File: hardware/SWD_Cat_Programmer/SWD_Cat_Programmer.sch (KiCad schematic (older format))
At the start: 19 parts

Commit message: Bom and footprints added
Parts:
- C1, C2, C3, C4, C5: renamed from C?; footprint (none) -> Capacitor_SMD:C_0603_1608Metric_Pad1.05x0.95mm_HandSolder
- D1: renamed from D?; footprint (none) -> LED_SMD:LED_0805_2012Metric
- J1: renamed from J?; footprint (none) -> Connector_PinHeader_2.54mm:PinHeader_2x05_P2.54mm_Vertical
- P1: renamed from P?; footprint (none) -> Connectors:C393939
- R1, R2, R3, R4, R5, R6, R7: renamed from R?; footprint (none) -> Resistor_SMD:R_0603_1608Metric_Pad1.05x0.95mm_HandSolder
- SW1, SW2: renamed from SW?; footprint (none) -> Button_Switch_SMD:SW_SPST_TL3342
- U1: renamed from U?; footprint (none) -> Package_SO:SOP-16_4.55x10.3mm_P1.27mm; symbol Electronic_Cats:CH552G -> SWD_Cat_Programmer-rescue:CH552G-Electronic_Cats
- gave numbers to parts that had none: 1

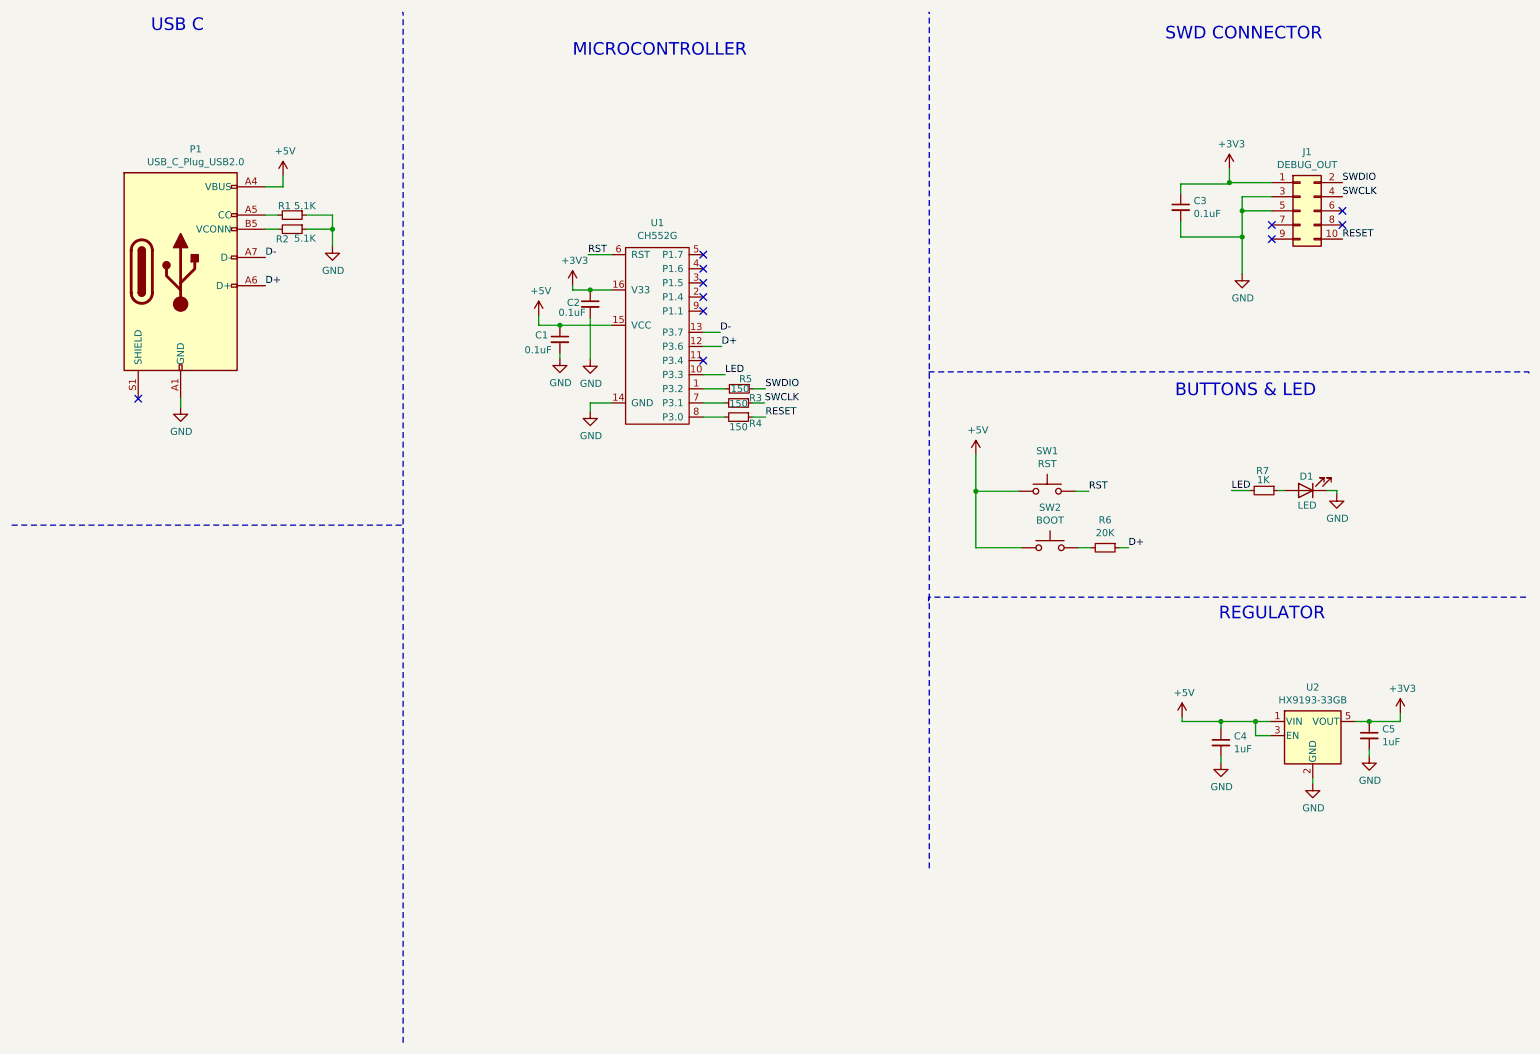
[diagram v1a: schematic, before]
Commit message: capacitors modified
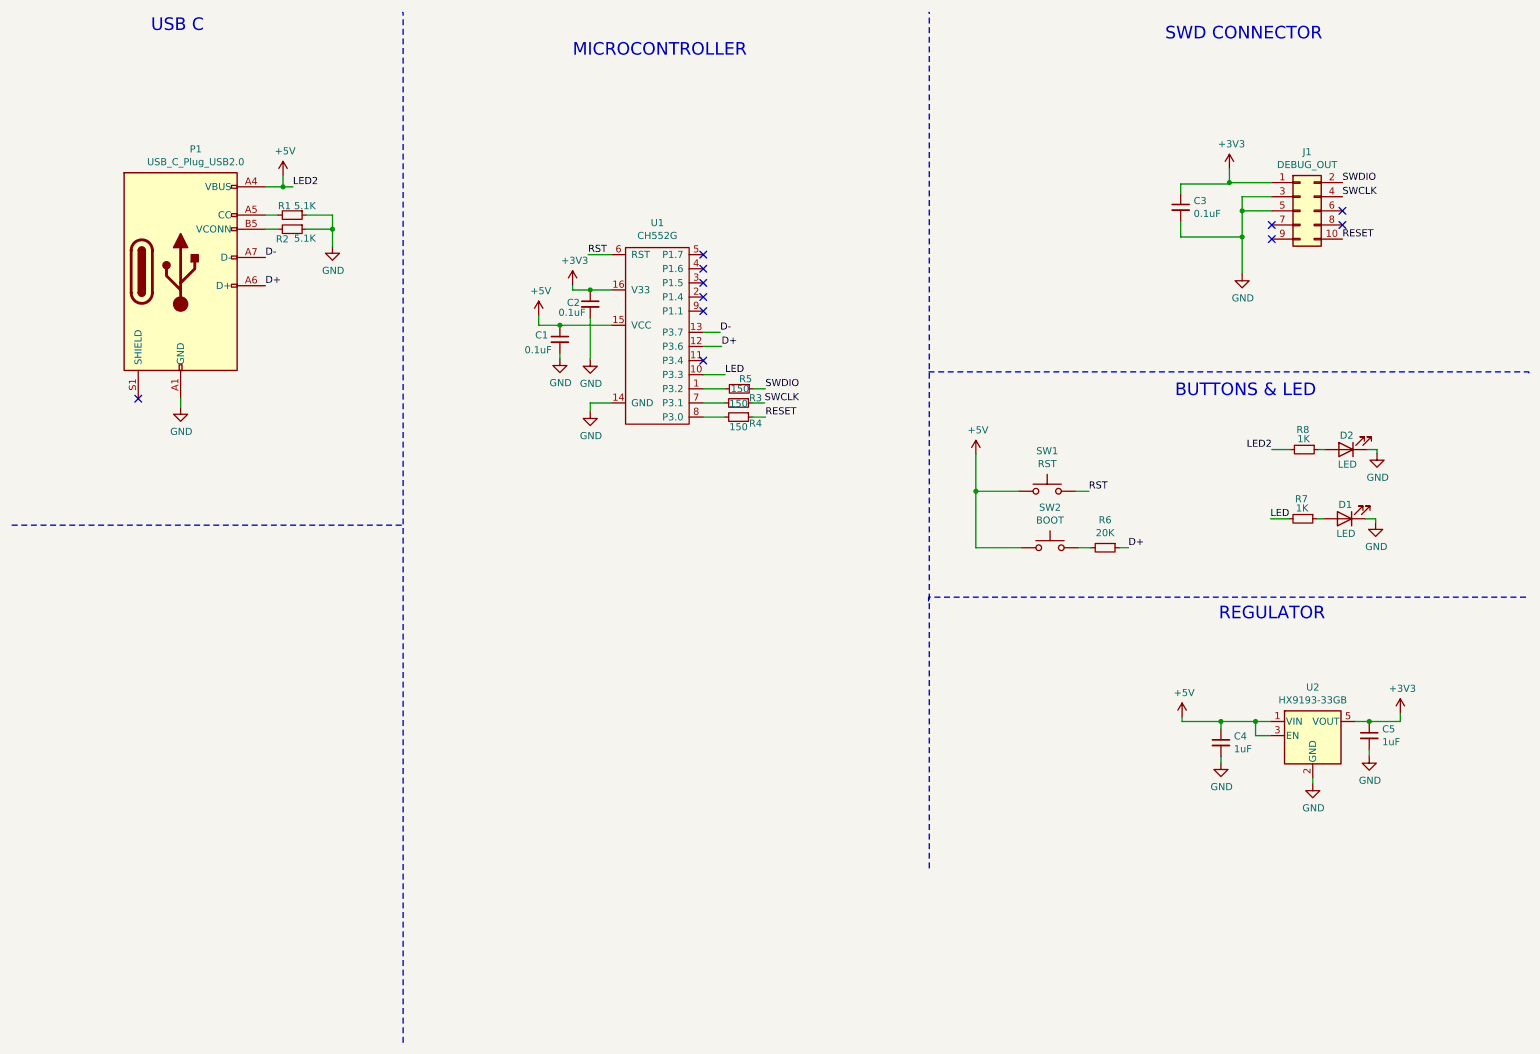
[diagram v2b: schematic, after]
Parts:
- added D2: LED, LED_SMD:LED_0805_2012Metric, symbol Device:LED
- added R8: 1K, Resistor_SMD:R_0805_2012Metric_Pad1.15x1.40mm_HandSolder, symbol Device:R_Small
- C1, C2, C3, C4, C5: footprint Capacitor_SMD:C_0603_1608Metric_Pad1.05x0.95mm_HandSolder -> Capacitor_SMD:C_0805_2012Metric_Pad1.15x1.40mm_HandSolder
- R1, R2, R3, R4, R5, R6, R7: footprint Resistor_SMD:R_0603_1608Metric_Pad1.05x0.95mm_HandSolder -> Resistor_SMD:R_0805_2012Metric_Pad1.15x1.40mm_HandSolder
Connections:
- net +5V: now also R8.2
- net GND: now also D2.1 (K)
- new net: D2.2 (A), R8.1
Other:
- moved on the sheet: D1, R7
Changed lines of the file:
@@
 F 0 "C3" H 8852 1901 50  0000 L CNN
 F 1 "0.1uF" H 8852 1810 50  0000 L CNN
-F 2 "Capacitor_SMD:C_0603_1608Metric_Pad1.05x0.95mm_HandSolder" H 8760 1855 50  0001 C CNN
+F 2 "Capacitor_SMD:C_0805_2012Metric_Pad1.15x1.40mm_HandSolder" H 8760 1855 50  0001 C CNN
 F 3 "~" H 8760 1855 50  0001 C CNN
 	1    8760 1855
@@
 F 0 "R1" V 2405 1855 50  0000 C CNN
 F 1 "5.1K" V 2405 2000 50  0000 C CNN
-F 2 "Resistor_SMD:R_0603_1608Metric_Pad1.05x0.95mm_HandSolder" H 2470 1910 50  0001 C CNN
+F 2 "Resistor_SMD:R_0805_2012Metric_Pad1.15x1.40mm_HandSolder" H 2470 1910 50  0001 C CNN
 F 3 "~" H 2470 1910 50  0001 C CNN
 	1    2470 1910
@@
 F 0 "C1" H 4190 2820 50  0000 L CNN
 F 1 "0.1uF" H 4115 2715 50  0000 L CNN
-F 2 "Capacitor_SMD:C_0603_1608Metric_Pad1.05x0.95mm_HandSolder" H 4365 2790 50  0001 C CNN
+F 2 "Capacitor_SMD:C_0805_2012Metric_Pad1.15x1.40mm_HandSolder" H 4365 2790 50  0001 C CNN
 F 3 "~" H 4365 2790 50  0001 C CNN
 	1    4365 2790
@@
 F 0 "C2" H 4415 2550 50  0000 L CNN
 F 1 "0.1uF" H 4355 2480 50  0000 L CNN
-F 2 "Capacitor_SMD:C_0603_1608Metric_Pad1.05x0.95mm_HandSolder" H 4580 2540 50  0001 C CNN
+F 2 "Capacitor_SMD:C_0805_2012Metric_Pad1.15x1.40mm_HandSolder" H 4580 2540 50  0001 C CNN
 F 3 "~" H 4580 2540 50  0001 C CNN
 	1    4580 2540
@@
 F 0 "R2" V 2540 1940 50  0000 C CNN
 F 1 "5.1K" V 2535 2100 50  0000 C CNN
-F 2 "Resistor_SMD:R_0603_1608Metric_Pad1.05x0.95mm_HandSolder" H 2470 2010 50  0001 C CNN
+F 2 "Resistor_SMD:R_0805_2012Metric_Pad1.15x1.40mm_HandSolder" H 2470 2010 50  0001 C CNN
 F 3 "~" H 2470 2010 50  0001 C CNN
 	1    2470 2010
@@
 $EndComp
 Wire Wire Line
-	9120 3860 9250 3860
+	9395 4060 9525 4060
 $Comp
 L Device:R_Small R7
 U 1 1 5F275B65
-P 9350 3860
-F 0 "R7" V 9210 3850 50  0000 C CNN
-F 1 "1K" V 9275 3855 50  0000 C CNN
-F 2 "Resistor_SMD:R_0603_1608Metric_Pad1.05x0.95mm_HandSolder" H 9350 3860 50  0001 C CNN
-F 3 "~" H 9350 3860 50  0001 C CNN
-	1    9350 3860
+P 9625 4060
+F 0 "R7" V 9485 4050 50  0000 C CNN
+F 1 "1K" V 9550 4055 50  0000 C CNN
+F 2 "Resistor_SMD:R_0805_2012Metric_Pad1.15x1.40mm_HandSolder" H 9625 4060 50  0001 C CNN
+F 3 "~" H 9625 4060 50  0001 C CNN
+	1    9625 4060
 	0    1    1    0
 $EndComp
@@
 L Device:LED D1
 U 1 1 5F2768D1
-P 9645 3860
-F 0 "D1" H 9640 3760 50  0000 C CNN
-F 1 "LED" H 9635 3965 50  0000 C CNN
-F 2 "LED_SMD:LED_0805_2012Metric" H 9645 3860 50  0001 C CNN
-F 3 "~" H 9645 3860 50  0001 C CNN
-	1    9645 3860
+P 9920 4060
+F 0 "D1" H 9915 3960 50  0000 C CNN
+F 1 "LED" H 9910 4165 50  0000 C CNN
+F 2 "LED_SMD:LED_0805_2012Metric" H 9920 4060 50  0001 C CNN
+F 3 "~" H 9920 4060 50  0001 C CNN
+	1    9920 4060
 	-1   0    0    1
 $EndComp
 Wire Wire Line
-	9450 3860 9495 3860
-Wire Wire Line
-	9795 3860 9865 3860
-Wire Wire Line
-	9865 3860 9865 3885
+	9725 4060 9770 4060
+Wire Wire Line
+	10070 4060 10140 4060
+Wire Wire Line
+	10140 4060 10140 4085
 $Comp
 L power:GND #PWR015
 U 1 1 5F277D50
-P 9865 3885
-F 0 "#PWR015" H 9865 3635 50  0001 C CNN
-F 1 "GND" H 9870 3712 50  0000 C CNN
-F 2 "" H 9865 3885 50  0001 C CNN
-F 3 "" H 9865 3885 50  0001 C CNN
-	1    9865 3885
+P 10140 4085
+F 0 "#PWR015" H 10140 3835 50  0001 C CNN
+F 1 "GND" H 10145 3912 50  0000 C CNN
+F 2 "" H 10140 4085 50  0001 C CNN
+F 3 "" H 10140 4085 50  0001 C CNN
+	1    10140 4085
 	1    0    0    -1
 $EndComp
@@
 F 0 "R6" V 8029 4265 50  0000 C CNN
 F 1 "20K" V 8120 4265 50  0000 C CNN
-F 2 "Resistor_SMD:R_0603_1608Metric_Pad1.05x0.95mm_HandSolder" H 8225 4265 50  0001 C CNN
+F 2 "Resistor_SMD:R_0805_2012Metric_Pad1.15x1.40mm_HandSolder" H 8225 4265 50  0001 C CNN
 F 3 "~" H 8225 4265 50  0001 C CNN
 	1    8225 4265
@@
 F 0 "R5" V 5565 3185 50  0000 C CNN
 F 1 "150" V 5635 3145 50  0000 C CNN
-F 2 "Resistor_SMD:R_0603_1608Metric_Pad1.05x0.95mm_HandSolder" H 5635 3140 50  0001 C CNN
+F 2 "Resistor_SMD:R_0805_2012Metric_Pad1.15x1.40mm_HandSolder" H 5635 3140 50  0001 C CNN
 F 3 "~" H 5635 3140 50  0001 C CNN
 	1    5635 3140
@@
 F 0 "R3" V 5595 3360 50  0000 C CNN
 F 1 "150" V 5635 3240 50  0000 C CNN
-F 2 "Resistor_SMD:R_0603_1608Metric_Pad1.05x0.95mm_HandSolder" H 5630 3240 50  0001 C CNN
+F 2 "Resistor_SMD:R_0805_2012Metric_Pad1.15x1.40mm_HandSolder" H 5630 3240 50  0001 C CNN
 F 3 "~" H 5630 3240 50  0001 C CNN
 	1    5630 3240
@@
 F 0 "R4" V 5675 3460 50  0000 C CNN
 F 1 "150" V 5700 3340 50  0000 C CNN
-F 2 "Resistor_SMD:R_0603_1608Metric_Pad1.05x0.95mm_HandSolder" H 5630 3340 50  0001 C CNN
+F 2 "Resistor_SMD:R_0805_2012Metric_Pad1.15x1.40mm_HandSolder" H 5630 3340 50  0001 C CNN
 F 3 "~" H 5630 3340 50  0001 C CNN
 	1    5630 3340
@@
 Text Label 5535 3040 0    50   ~ 0
 LED
-Text Label 9120 3860 0    50   ~ 0
+Text Label 9395 4060 0    50   ~ 0
 LED
 NoConn ~ 5380 2190
@@
 F 0 "C4" H 9137 5691 50  0000 L CNN
 F 1 "1uF" H 9137 5600 50  0000 L CNN
-F 2 "Capacitor_SMD:C_0603_1608Metric_Pad1.05x0.95mm_HandSolder" H 9045 5645 50  0001 C CNN
+F 2 "Capacitor_SMD:C_0805_2012Metric_Pad1.15x1.40mm_HandSolder" H 9045 5645 50  0001 C CNN
 F 3 "~" H 9045 5645 50  0001 C CNN
 	1    9045 5645
@@
 F 0 "C5" H 10187 5641 50  0000 L CNN
 F 1 "1uF" H 10187 5550 50  0000 L CNN
-F 2 "Capacitor_SMD:C_0603_1608Metric_Pad1.05x0.95mm_HandSolder" H 10095 5595 50  0001 C CNN
+F 2 "Capacitor_SMD:C_0805_2012Metric_Pad1.15x1.40mm_HandSolder" H 10095 5595 50  0001 C CNN
 F 3 "~" H 10095 5595 50  0001 C CNN
 	1    10095 5595
@@
 	1    0    0    -1
 $EndComp
-Wire Wire Line
-	2280 1710 2405 1710
-Wire Wire Line
-	2405 1710 2405 1630
 NoConn ~ 1380 3210
 NoConn ~ 5380 2940
@@
 	1    0    0    -1
 $EndComp
+Wire Wire Line
+	9405 3570 9535 3570
+$Comp
+L Device:R_Small R8
+U 1 1 5F2A19DA
+P 9635 3570
+F 0 "R8" V 9495 3560 50  0000 C CNN
+F 1 "1K" V 9560 3565 50  0000 C CNN
+F 2 "Resistor_SMD:R_0805_2012Metric_Pad1.15x1.40mm_HandSolder" H 9635 3570 50  0001 C CNN
+F 3 "~" H 9635 3570 50  0001 C CNN
+	1    9635 3570
+	0    1    1    0
+$EndComp
+$Comp
+L Device:LED D2
+U 1 1 5F2A19E0
+P 9930 3570
+F 0 "D2" H 9925 3470 50  0000 C CNN
+F 1 "LED" H 9920 3675 50  0000 C CNN
+F 2 "LED_SMD:LED_0805_2012Metric" H 9930 3570 50  0001 C CNN
+F 3 "~" H 9930 3570 50  0001 C CNN
+	1    9930 3570
+	-1   0    0    1
+$EndComp
+Wire Wire Line
+	9735 3570 9780 3570
+Wire Wire Line
+	10080 3570 10150 3570
+Wire Wire Line
+	10150 3570 10150 3595
+$Comp
+L power:GND #PWR0101
+U 1 1 5F2A19E9
+P 10150 3595
+F 0 "#PWR0101" H 10150 3345 50  0001 C CNN
+F 1 "GND" H 10155 3422 50  0000 C CNN
+F 2 "" H 10150 3595 50  0001 C CNN
+F 3 "" H 10150 3595 50  0001 C CNN
+	1    10150 3595
+	1    0    0    -1
+$EndComp
+Text Label 9405 3570 2    50   ~ 0
+LED2
+Text Label 2475 1710 0    50   ~ 0
+LED2
+Wire Wire Line
+	2280 1710 2405 1710
+Wire Wire Line
+	2405 1630 2405 1710
+Connection ~ 2405 1710
+Wire Wire Line
+	2405 1710 2475 1710
 $EndSCHEMATC

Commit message: PCB
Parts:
- J1: footprint Connector_PinHeader_2.54mm:PinHeader_2x05_P2.54mm_Vertical -> Connector_PinHeader_2.54mm:PinHeader_2x05_P2.54mm_Horizontal
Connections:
- net GND: now also P1.S1 (SHIELD)
- no-connect marks 11 -> 10
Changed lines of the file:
@@
 F 0 "J1" H 9655 2297 50  0000 C CNN
 F 1 "DEBUG_OUT" H 9655 2206 50  0000 C CNN
-F 2 "Connector_PinHeader_2.54mm:PinHeader_2x05_P2.54mm_Vertical" H 9605 1880 50  0001 C CNN
+F 2 "Connector_PinHeader_2.54mm:PinHeader_2x05_P2.54mm_Horizontal" H 9605 1880 50  0001 C CNN
 F 3 "~" H 9605 1880 50  0001 C CNN
 	1    9605 1880
@@
 	2280 2010 2370 2010
 Wire Wire Line
-	1680 3210 1680 3270
+	1680 3210 1680 3245
 $Comp
 L power:GND #PWR01
@@
 	1    0    0    -1
 $EndComp
-NoConn ~ 1380 3210
 NoConn ~ 5380 2940
 $Comp
@@
 Wire Wire Line
 	2405 1710 2475 1710
+Wire Wire Line
+	1380 3210 1380 3245
+Wire Wire Line
+	1380 3245 1680 3245
+Connection ~ 1680 3245
+Wire Wire Line
+	1680 3245 1680 3270
 $EndSCHEMATC

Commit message: buttons changed
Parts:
- SW1, SW2: footprint Button_Switch_SMD:SW_SPST_TL3342 -> KiCad:TS1088R02026
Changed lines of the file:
@@
 F 0 "SW1" H 7815 4150 50  0000 C CNN
 F 1 "RST" H 7815 4059 50  0000 C CNN
-F 2 "Button_Switch_SMD:SW_SPST_TL3342" H 7815 4065 50  0001 C CNN
+F 2 "KiCad:TS1088R02026" H 7815 4065 50  0001 C CNN
 F 3 "~" H 7815 4065 50  0001 C CNN
 	1    7815 3865
@@
 F 0 "SW2" H 7835 4550 50  0000 C CNN
 F 1 "BOOT" H 7835 4459 50  0000 C CNN
-F 2 "Button_Switch_SMD:SW_SPST_TL3342" H 7835 4465 50  0001 C CNN
+F 2 "KiCad:TS1088R02026" H 7835 4465 50  0001 C CNN
 F 3 "~" H 7835 4465 50  0001 C CNN
 	1    7835 4265

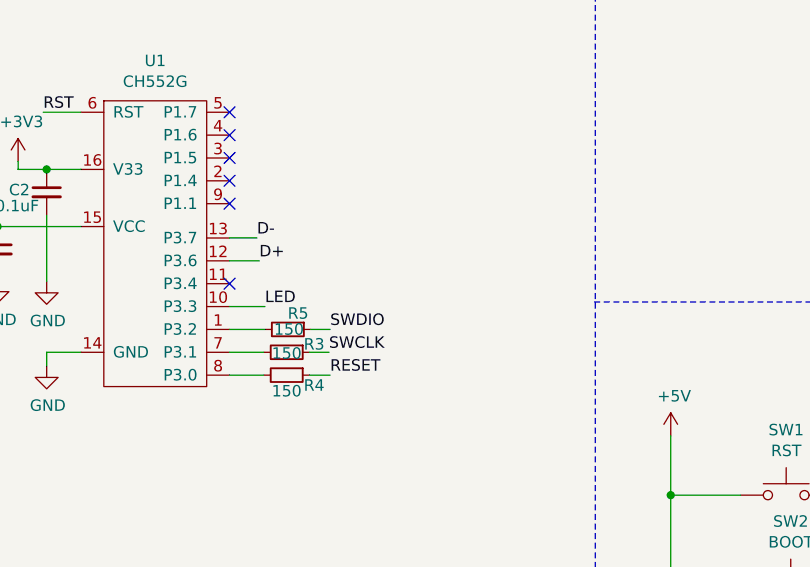
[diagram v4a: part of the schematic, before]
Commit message: Pull up Resistors Update
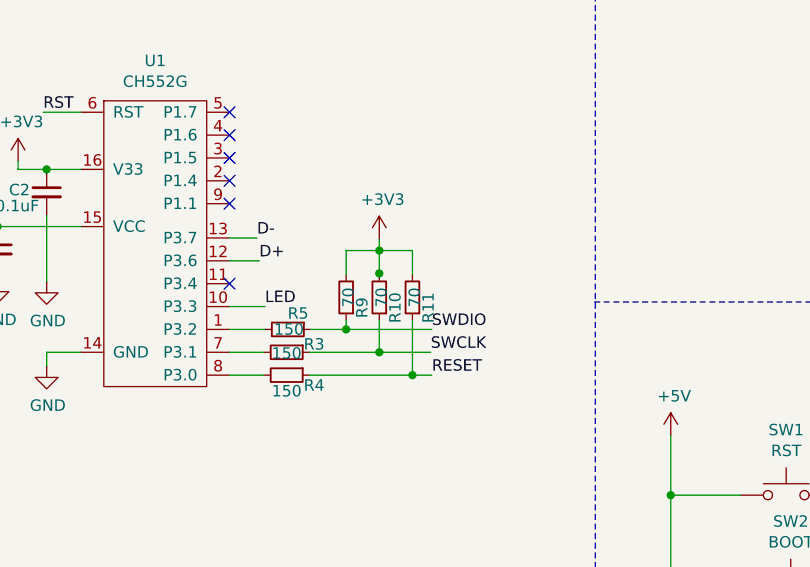
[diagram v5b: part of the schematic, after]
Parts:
- added R10, R11, R9: 70, Resistor_SMD:R_0603_1608Metric_Pad1.05x0.95mm_HandSolder, symbol Device:R_Small
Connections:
- net +3V3: now also R10.2, R11.2, R9.2
- net RESET: now also R11.1
- net SWCLK: now also R10.1
- net SWDIO: now also R9.1
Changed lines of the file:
@@
 Wire Wire Line
 	5380 3140 5535 3140
-Text Label 5820 3140 0    50   ~ 0
+Text Label 6265 3140 0    50   ~ 0
 SWDIO
-Text Label 5815 3240 0    50   ~ 0
+Text Label 6260 3240 0    50   ~ 0
 SWCLK
-Text Label 5820 3340 0    50   ~ 0
+Text Label 6265 3340 0    50   ~ 0
 RESET
 $Comp
@@
 	0    1    1    0
 $EndComp
-Wire Wire Line
-	5730 3240 5815 3240
-Wire Wire Line
-	5730 3340 5820 3340
-Wire Wire Line
-	5735 3140 5820 3140
 Wire Wire Line
 	5380 3040 5535 3040
@@
 Wire Wire Line
 	1680 3245 1680 3270
+$Comp
+L Device:R_Small R9
+U 1 1 5F37508C
+P 5890 3000
+F 0 "R9" V 5820 3045 50  0000 C CNN
+F 1 "70" V 5880 3000 50  0000 C CNN
+F 2 "Resistor_SMD:R_0603_1608Metric_Pad1.05x0.95mm_HandSolder" H 5890 3000 50  0001 C CNN
+F 3 "~" H 5890 3000 50  0001 C CNN
+	1    5890 3000
+	-1   0    0    1
+$EndComp
+$Comp
+L Device:R_Small R10
+U 1 1 5F3755BC
+P 6035 3000
+F 0 "R10" V 5965 3045 50  0000 C CNN
+F 1 "70" V 6025 3000 50  0000 C CNN
+F 2 "Resistor_SMD:R_0603_1608Metric_Pad1.05x0.95mm_HandSolder" H 6035 3000 50  0001 C CNN
+F 3 "~" H 6035 3000 50  0001 C CNN
+	1    6035 3000
+	-1   0    0    1
+$EndComp
+$Comp
+L Device:R_Small R11
+U 1 1 5F375902
+P 6180 3000
+F 0 "R11" V 6110 3045 50  0000 C CNN
+F 1 "70" V 6170 3000 50  0000 C CNN
+F 2 "Resistor_SMD:R_0603_1608Metric_Pad1.05x0.95mm_HandSolder" H 6180 3000 50  0001 C CNN
+F 3 "~" H 6180 3000 50  0001 C CNN
+	1    6180 3000
+	-1   0    0    1
+$EndComp
+Wire Wire Line
+	5735 3140 5890 3140
+Wire Wire Line
+	5730 3240 6035 3240
+Wire Wire Line
+	5730 3340 6180 3340
+Wire Wire Line
+	5890 3100 5890 3140
+Connection ~ 5890 3140
+Wire Wire Line
+	5890 3140 6265 3140
+Wire Wire Line
+	6035 3100 6035 3240
+Connection ~ 6035 3240
+Wire Wire Line
+	6035 3240 6260 3240
+Wire Wire Line
+	6180 3100 6180 3340
+Connection ~ 6180 3340
+Wire Wire Line
+	6180 3340 6265 3340
+$Comp
+L power:+3V3 #PWR018
+U 1 1 5F387CBC
+P 6035 2745
+F 0 "#PWR018" H 6035 2595 50  0001 C CNN
+F 1 "+3V3" H 6050 2918 50  0000 C CNN
+F 2 "" H 6035 2745 50  0001 C CNN
+F 3 "" H 6035 2745 50  0001 C CNN
+	1    6035 2745
+	1    0    0    -1
+$EndComp
+Wire Wire Line
+	5890 2900 5890 2795
+Wire Wire Line
+	5890 2795 6035 2795
+Wire Wire Line
+	6180 2795 6180 2900
+Connection ~ 6035 2795
+Wire Wire Line
+	6035 2795 6180 2795
+Wire Wire Line
+	6035 2795 6035 2745
+Connection ~ 6035 2895
+Wire Wire Line
+	6035 2795 6035 2900
 $EndSCHEMATC

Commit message: jumper voltage
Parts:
- added JP1: Jumper, symbol Jumper:Jumper_3_Bridged12
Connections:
- net +3V3: now also JP1.1 (A)
- net +5V: now also JP1.3 (B); no longer C1.1, U1.15 (VCC)
- new net: C1.1, JP1.2 (C), U1.15 (VCC)
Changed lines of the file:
@@
 Sheet 1 1
 Title "CMIS DAP Cat Programmer"
-Date "2020-08-02"
+Date "2020-08-07"
 Rev "1.0"
 Comp "Electronic Cats"
 Comment1 ""
-Comment2 ""
-Comment3 ""
+Comment2 "Eduaro Wero"
+Comment3 "Felipe Islas"
 Comment4 "Andres Sabas"
 $EndDescr
@@
 Wire Wire Line
 	4730 2690 4365 2690
-Wire Wire Line
-	4215 2690 4215 2620
 $Comp
 L power:+3V3 #PWR06
@@
 L power:+5V #PWR04
 U 1 1 5F26D6C6
-P 4215 2620
-F 0 "#PWR04" H 4215 2470 50  0001 C CNN
-F 1 "+5V" H 4230 2793 50  0000 C CNN
-F 2 "" H 4215 2620 50  0001 C CNN
-F 3 "" H 4215 2620 50  0001 C CNN
-	1    4215 2620
+P 3835 2315
+F 0 "#PWR04" H 3835 2165 50  0001 C CNN
+F 1 "+5V" H 3850 2488 50  0000 C CNN
+F 2 "" H 3835 2315 50  0001 C CNN
+F 3 "" H 3835 2315 50  0001 C CNN
+	1    3835 2315
 	1    0    0    -1
 $EndComp
@@
 Connection ~ 4580 2440
 Wire Wire Line
-	4580 2440 4455 2440
+	4580 2440 4465 2440
 Wire Wire Line
 	4580 2640 4580 2930
@@
 Wire Wire Line
 	6035 2795 6035 2745
-Connection ~ 6035 2895
 Wire Wire Line
 	6035 2795 6035 2900
+$Comp
+L Jumper:Jumper_3_Bridged12 JP1
+U 1 1 5F2F87B3
+P 4215 2440
+F 0 "JP1" H 4215 2644 50  0000 C CNN
+F 1 "Jumper" H 4215 2553 50  0000 C CNN
+F 2 "" H 4215 2440 50  0001 C CNN
+F 3 "~" H 4215 2440 50  0001 C CNN
+	1    4215 2440
+	-1   0    0    -1
+$EndComp
+Connection ~ 4465 2440
+Wire Wire Line
+	4465 2440 4455 2440
+Wire Wire Line
+	4215 2590 4215 2690
+Wire Wire Line
+	3965 2440 3835 2440
+Wire Wire Line
+	3835 2440 3835 2315
 $EndSCHEMATC

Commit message: Jumper
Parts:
- JP1: footprint (none) -> Jumper:SolderJumper-3_P1.3mm_Bridged12_RoundedPad1.0x1.5mm
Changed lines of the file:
@@
 F 0 "JP1" H 4215 2644 50  0000 C CNN
 F 1 "Jumper" H 4215 2553 50  0000 C CNN
-F 2 "" H 4215 2440 50  0001 C CNN
+F 2 "Jumper:SolderJumper-3_P1.3mm_Bridged12_RoundedPad1.0x1.5mm" H 4215 2440 50  0001 C CNN
 F 3 "~" H 4215 2440 50  0001 C CNN
 	1    4215 2440
